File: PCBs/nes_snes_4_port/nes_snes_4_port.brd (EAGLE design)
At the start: 72.9 x 73.2 mm, 40 parts, among them J5 RJ45, J6 RJ45, J7 RJ45, J8 RJ45, J9 RJ45-S-4, U1 74245, U10 MC74VHC1GT125, U2 MC74VHC1GT125, U3 MC74VHC1GT125, U4 MC74VHC1GT125, U5 MC74VHC1GT125, U7 MC74VHC1GT125, U8 MC74VHC1GT125, U9 MC74VHC1GT125

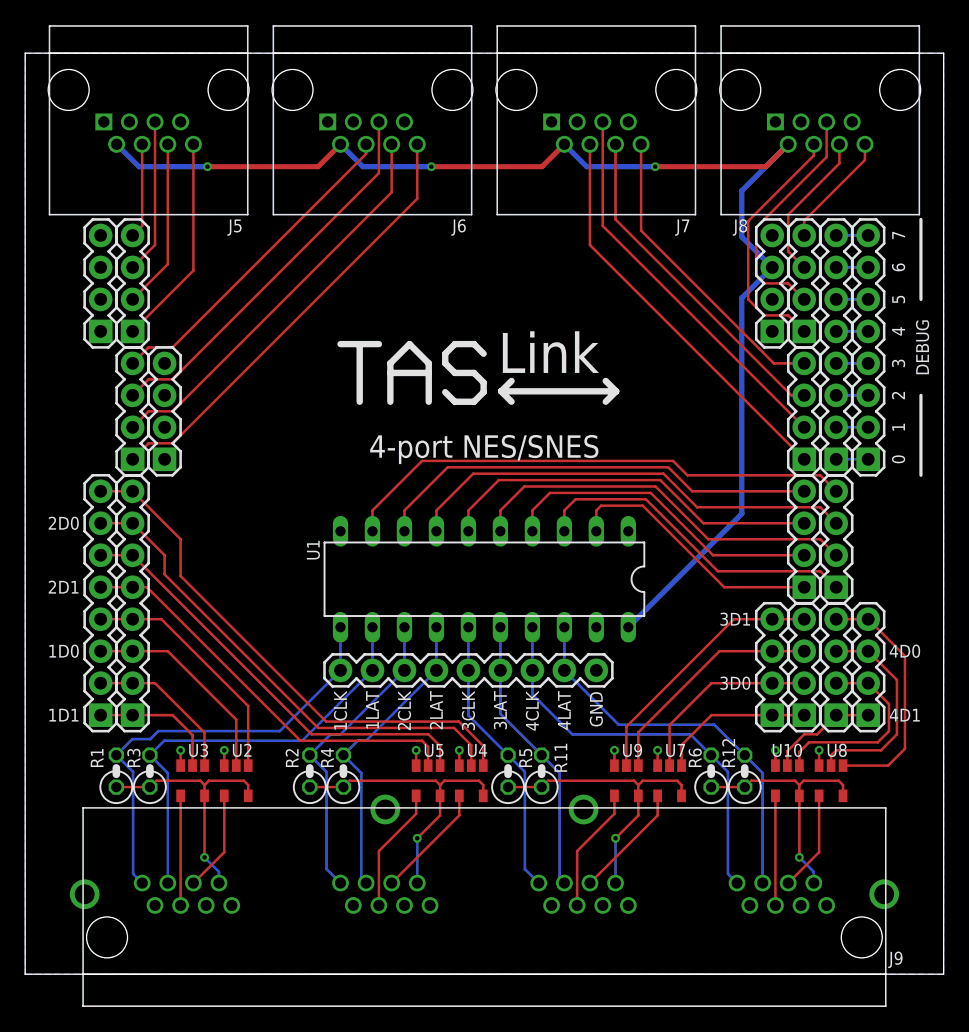
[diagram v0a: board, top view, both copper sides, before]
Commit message: 4 port PCB: Added decoupling capacitors.
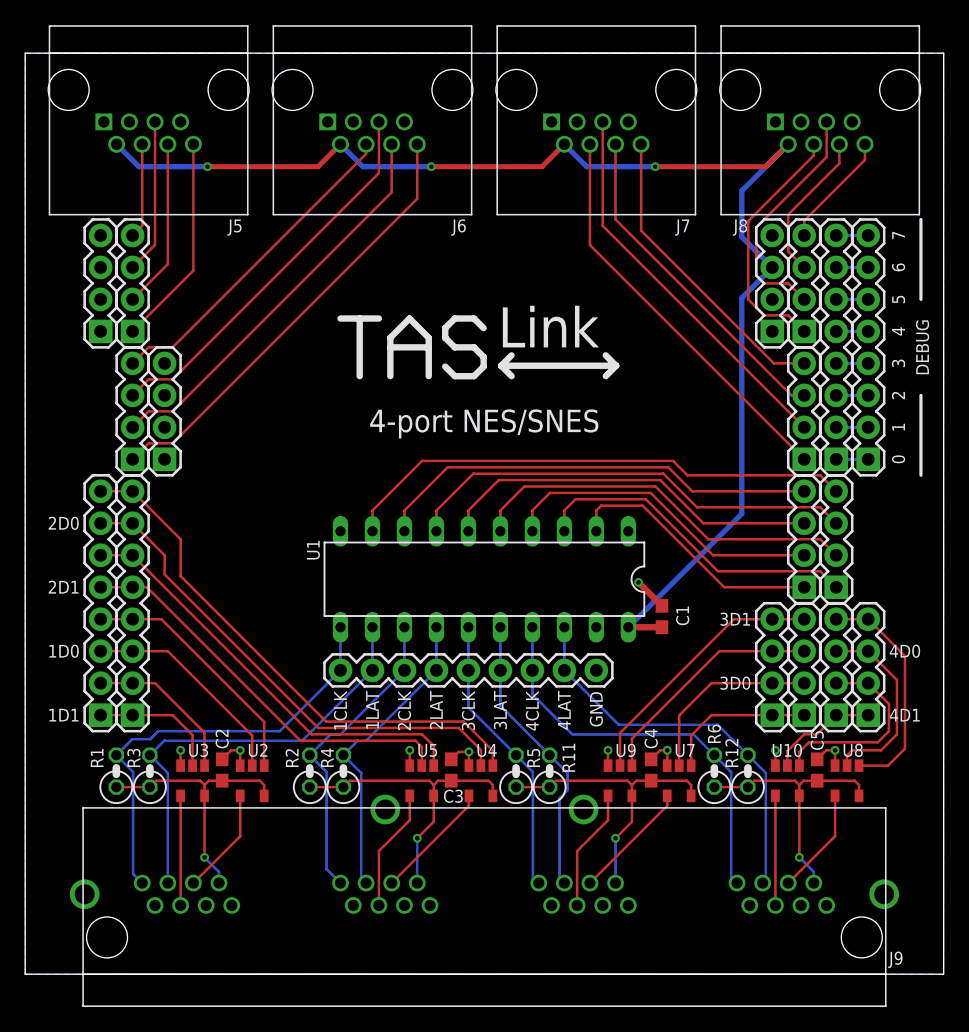
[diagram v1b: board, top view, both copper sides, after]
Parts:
- added C1, C2, C3, C4, C5: 0.1u, rcl:C0603
- moved U2 1.27 mm to (18.4, 15.4)
- moved U8 1.27 mm to (65.6, 15.4)
- moved U4 0.76 mm to (36.6, 15.4)
- moved U7 0.76 mm to (52.3, 15.4)
- moved R11 0.63 mm to (42.0, 16.1)
- moved R5 0.63 mm to (39.3, 16.1)
- moved U5 0.51 mm to (31.9, 15.4)
- moved U9 0.51 mm to (47.6, 15.4)
- moved R12 0.25 mm to (57.8, 16.1)
- moved R6 0.25 mm to (55.1, 16.1)
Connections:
- net +3V3: now also C1.1
- net CP1_+5V: now also C2.1
- net CP2_+5V: now also C3.1
- net CP3_+5V: now also C4.1
- net CP4_+5V: now also C5.1
- net GND: now also C1.2, C2.2, C3.2, C4.2, C5.2
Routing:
- net GND: track 9.70 -> 18.9 mm, vias 8 -> 9
- net +3V3: track 103.4 -> 106.0 mm
- net CP4_D0_OE_LV: track 19.5 -> 18.2 mm
- net CP4_DO_LV: track 16.8 -> 15.6 mm
- net CP1_+5V: track 20.2 -> 21.5 mm
- net CP4_+5V: track 20.2 -> 21.2 mm
- net CP2_+5V: track 23.8 -> 24.4 mm
- net CP2_DO_LV: track 39.3 -> 39.8 mm
- net CP2_D0_OE_LV: track 42.0 -> 42.6 mm
- net CP1_D0_LV: track 16.7 -> 17.2 mm
- net CP1_D0_OE_LV: track 19.3 -> 19.8 mm
- net CP1_D0: track 7.94 -> 8.47 mm
- net CP4_D0: track 7.94 -> 8.47 mm
- net CP3_LATCH: track 22.4 -> 23.0 mm
- net CP2_D1_OE_LV: track 34.8 -> 34.3 mm
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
